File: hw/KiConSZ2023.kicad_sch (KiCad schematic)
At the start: 0 parts

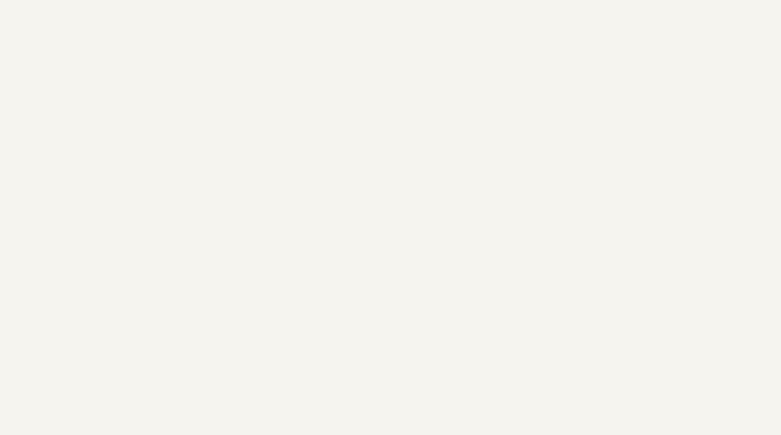
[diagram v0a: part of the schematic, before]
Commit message: USB Type-C Connector
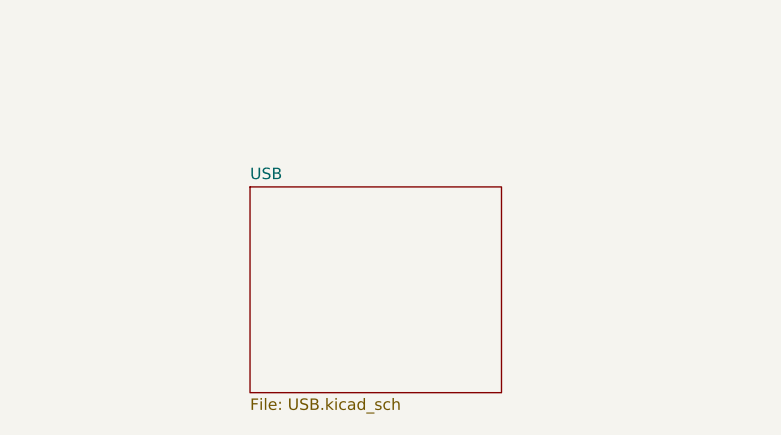
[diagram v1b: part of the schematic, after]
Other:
- added sheet USB (USB.kicad_sch)
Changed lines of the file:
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@@
     (effects (font (size 1.27 1.27)) (justify left bottom))
+  )
+  (sheet (at 45.72 167.64) (size 27.94 22.86) (fields_autoplaced)
+    (stroke (width 0.1524) (type solid))
+    (fill (color 0 0 0 0.0000))
+    (property "Sheetname" "USB" (at 45.72 166.9284 0)
+      (effects (font (size 1.27 1.27)) (justify left bottom))
+    )
+    (property "Sheetfile" "USB.kicad_sch" (at 45.72 191.0846 0)
+      (effects (font (size 1.27 1.27)) (justify left top))
+    )
+    (instances
+      (project "KiConSZ2023"
+        (path "/8659c260-f029-4e72-8b9a-85fff45eea40" (page "58"))
+      )
+    )
   )
   (sheet (at 177.8 48.26) (size 63.5 68.58) (fields_autoplaced)

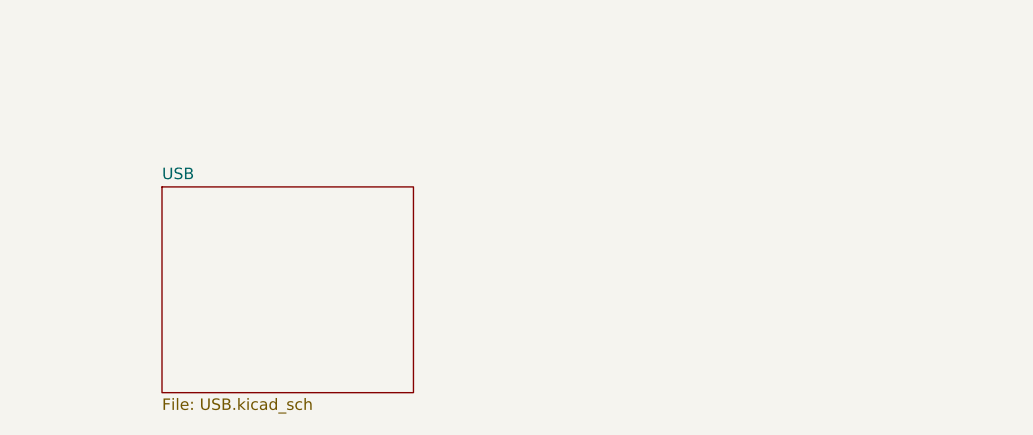
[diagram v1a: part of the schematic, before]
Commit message: added Buck Converter
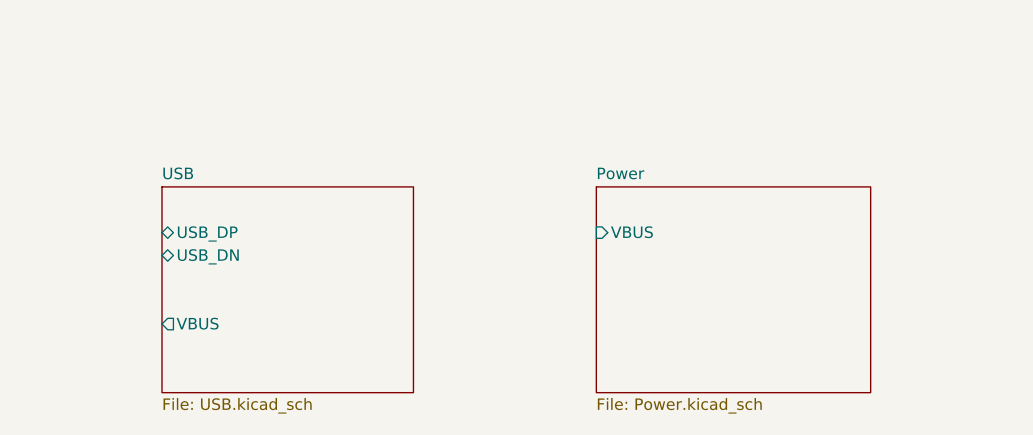
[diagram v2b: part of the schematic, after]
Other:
- added sheet Power (Power.kicad_sch)
- sheet USB ports: added USB_DN, USB_DP, VBUS; removed none
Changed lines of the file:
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@@
       (effects (font (size 1.27 1.27)) (justify left top))
+    )
+    (pin "USB_DP" bidirectional (at 45.72 172.72 180)
+      (effects (font (size 1.27 1.27)) (justify left))
+    )
+    (pin "VBUS" output (at 45.72 182.88 180)
+      (effects (font (size 1.27 1.27)) (justify left))
+    )
+    (pin "USB_DN" bidirectional (at 45.72 175.26 180)
+      (effects (font (size 1.27 1.27)) (justify left))
     )
     (instances
@@
       )
     )
+  )
+  (sheet (at 93.98 167.64) (size 30.48 22.86) (fields_autoplaced)
+    (stroke (width 0.1524) (type solid))
+    (fill (color 0 0 0 0.0000))
+    (property "Sheetname" "Power" (at 93.98 166.9284 0)
+      (effects (font (size 1.27 1.27)) (justify left bottom))
+    )
+    (property "Sheetfile" "Power.kicad_sch" (at 93.98 191.0846 0)
+      (effects (font (size 1.27 1.27)) (justify left top))
+    )
+    (pin "VBUS" input (at 93.98 172.72 180)
+      (effects (font (size 1.27 1.27)) (justify left))
+    )
+    (instances
+      (project "KiConSZ2023"
+        (path "/8659c260-f029-4e72-8b9a-85fff45eea40" (page "59"))
+      )
+    )

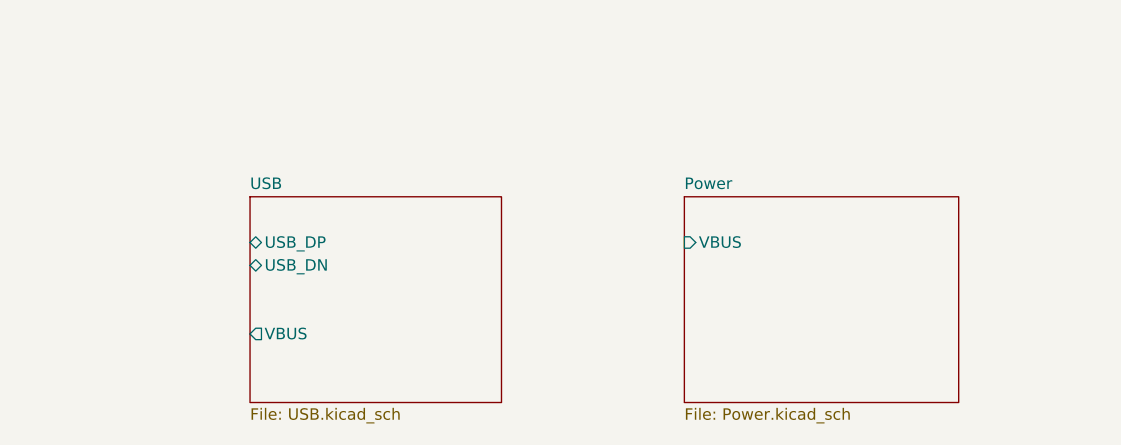
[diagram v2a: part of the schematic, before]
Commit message: added switches
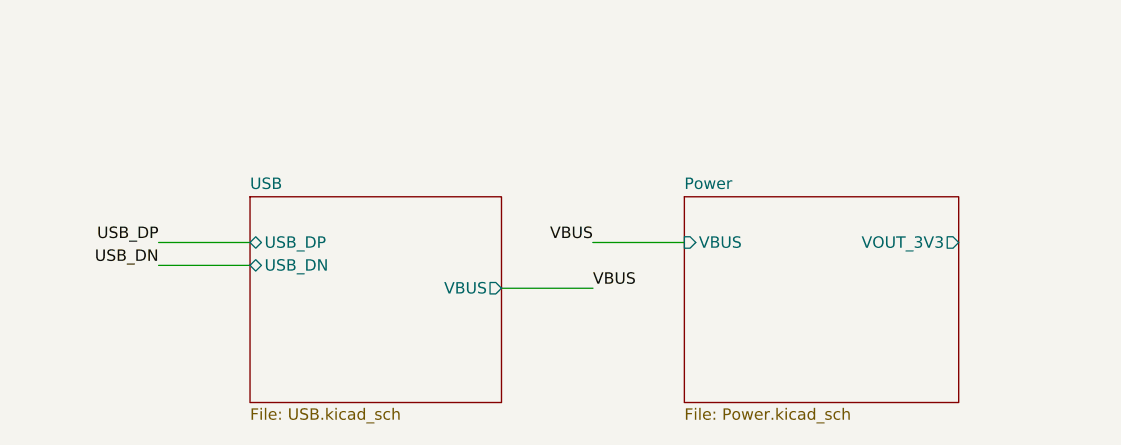
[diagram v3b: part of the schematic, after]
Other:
- sheet Power ports: added VOUT_3V3; removed none
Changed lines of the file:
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@@
+    (stroke (width 0) (type default))
+  )
+  (wire (pts (xy 45.72 175.26) (xy 35.56 175.26))
     (stroke (width 0) (type default))
   )
@@
     (stroke (width 0) (type default))
   )
+  (wire (pts (xy 83.82 172.72) (xy 93.98 172.72))
+    (stroke (width 0) (type default))
+  )
   (wire (pts (xy 241.3 106.68) (xy 248.92 106.68))
     (stroke (width 0) (type default))
@@
     (stroke (width 0) (type default))
   )
+  (wire (pts (xy 45.72 172.72) (xy 35.56 172.72))
+    (stroke (width 0) (type default))
+  )
   (wire (pts (xy 97.79 99.06) (xy 106.68 99.06))
     (stroke (width 0) (type default))
@@
     (stroke (width 0) (type default))
   )
+  (wire (pts (xy 83.82 177.8) (xy 73.66 177.8))
+    (stroke (width 0) (type default))
+  )
   (wire (pts (xy 43.18 96.52) (xy 33.02 96.52))
     (stroke (width 0) (type default))
@@
     (effects (font (size 1.27 1.27)) (justify left bottom))
   )
+  (label "USB_DN" (at 35.56 175.26 180) (fields_autoplaced)
+    (effects (font (size 1.27 1.27)) (justify right bottom))
+  )
+  (label "VBUS" (at 83.82 172.72 180) (fields_autoplaced)
+    (effects (font (size 1.27 1.27)) (justify right bottom))
+  )
   (label "DISP_SCK" (at 33.02 76.2 180) (fields_autoplaced)
     (effects (font (size 1.27 1.27)) (justify right bottom))
   )
+  (label "VBUS" (at 83.82 177.8 0) (fields_autoplaced)
+    (effects (font (size 1.27 1.27)) (justify left bottom))
+  )
   (label "LowSide_Input_B_Col_6" (at 106.68 132.08 0) (fields_autoplaced)
     (effects (font (size 1.27 1.27)) (justify left bottom))
@@
   (label "LowSide_Input_R_Col_2" (at 106.68 86.36 0) (fields_autoplaced)
     (effects (font (size 1.27 1.27)) (justify left bottom))
+  )
+  (label "USB_DP" (at 35.56 172.72 180) (fields_autoplaced)
+    (effects (font (size 1.27 1.27)) (justify right bottom))
   )
   (label "LowSide_Input_G_Col_1" (at 105.41 78.74 0) (fields_autoplaced)
@@
       (effects (font (size 1.27 1.27)) (justify left))
     )
-    (pin "VBUS" output (at 45.72 182.88 180)
-      (effects (font (size 1.27 1.27)) (justify left))
+    (pin "VBUS" output (at 73.66 177.8 0)
+      (effects (font (size 1.27 1.27)) (justify right))
     )
     (pin "USB_DN" bidirectional (at 45.72 175.26 180)
@@
       (effects (font (size 1.27 1.27)) (justify left))
     )
+    (pin "VOUT_3V3" output (at 124.46 172.72 0)
+      (effects (font (size 1.27 1.27)) (justify right))
+    )
     (instances

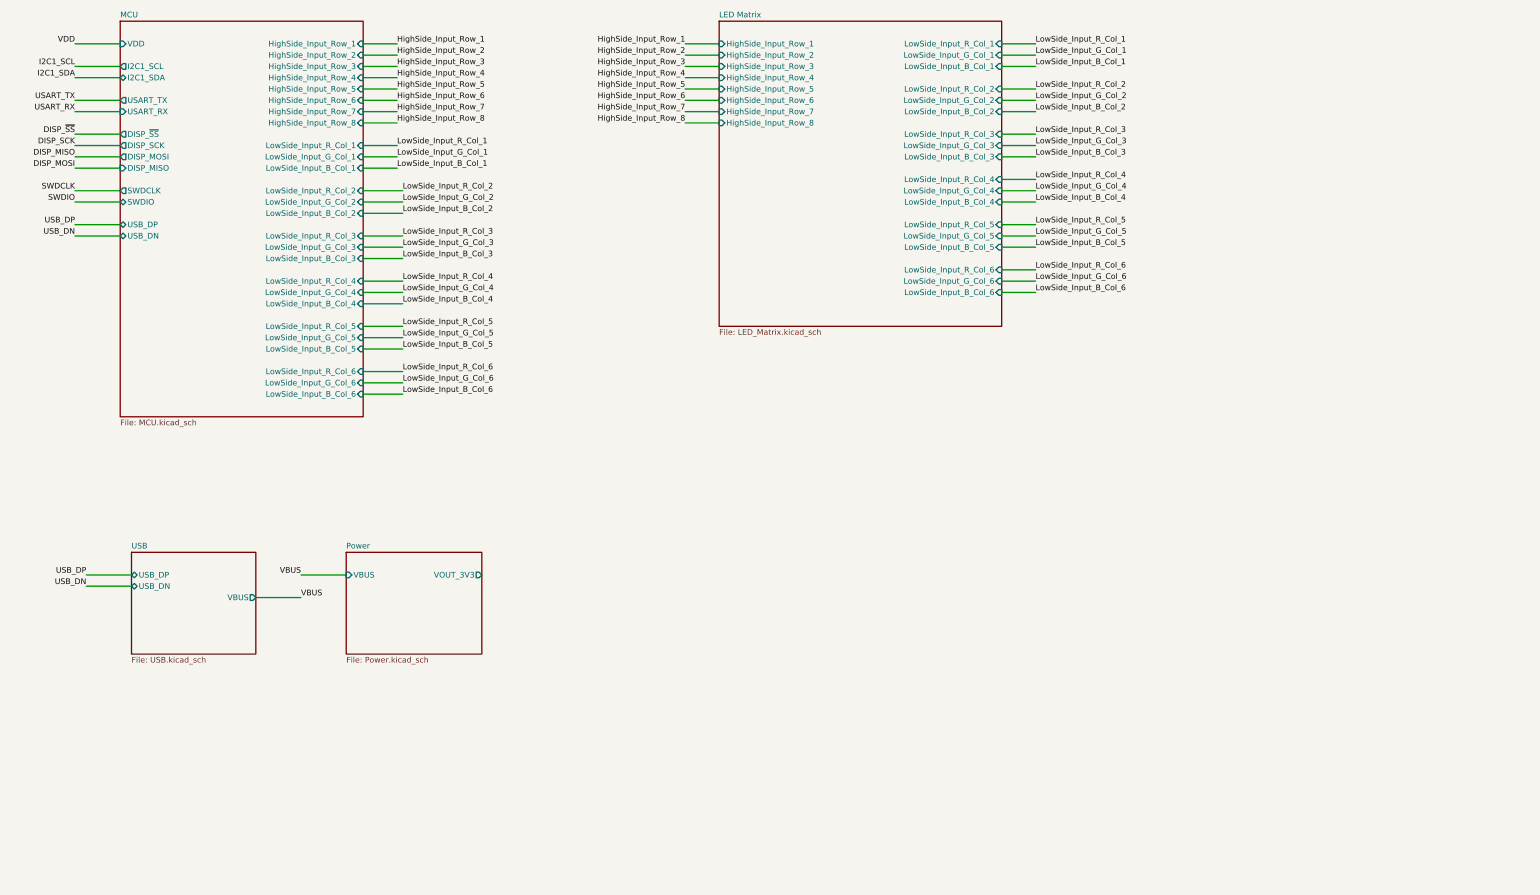
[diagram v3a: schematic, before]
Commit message: changed connections and ports
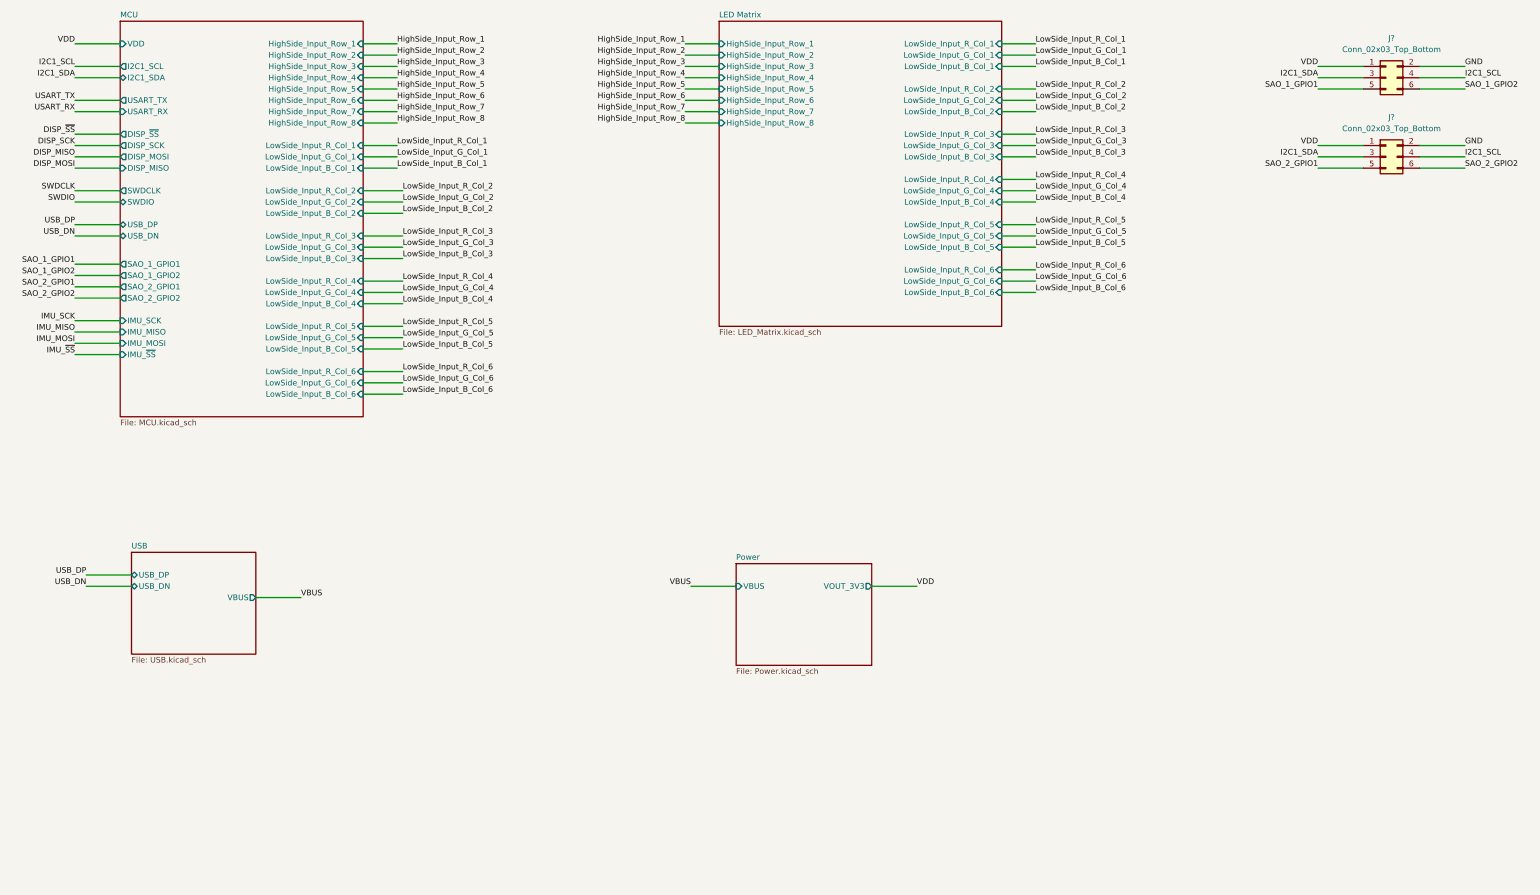
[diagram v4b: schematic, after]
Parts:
- added J? (x2): Conn_02x03_Top_Bottom, symbol Connector_Generic:Conn_02x03_Odd_Even
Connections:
- net I2C1_SCL: now also J?.4 (Pin_4), J?.4 (Pin_4)
- net I2C1_SDA: now also J?.3 (Pin_3), J?.3 (Pin_3)
- net VDD: now also J?.1 (Pin_1), J?.1 (Pin_1)
- new net GND: J?.2 (Pin_2), J?.2 (Pin_2)
- new net SAO_1_GPIO1: J?.5 (Pin_5)
- new net SAO_1_GPIO2: J?.6 (Pin_6)
- new net SAO_2_GPIO1: J?.5 (Pin_5)
- new net SAO_2_GPIO2: J?.6 (Pin_6)
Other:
- sheet MCU ports: added IMU_MISO, IMU_MOSI, IMU_SCK, IMU_~{SS}, SAO_1_GPIO1, SAO_1_GPIO2, SAO_2_GPIO1, SAO_2_GPIO2; removed none

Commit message: setup footprints of 02x03 SAO connectors
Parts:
- J? (x2): footprint (none) -> Connector_PinSocket_2.54mm:PinSocket_2x03_P2.54mm_Vertical
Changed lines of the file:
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@@
       (effects (font (size 1.27 1.27)))
     )
-    (property "Footprint" "" (at 327.66 78.74 0)
+    (property "Footprint" "Connector_PinSocket_2.54mm:PinSocket_2x03_P2.54mm_Vertical" (at 327.66 78.74 0)
       (effects (font (size 1.27 1.27)) hide)
     )
@@
       (effects (font (size 1.27 1.27)))
     )
-    (property "Footprint" "" (at 327.66 60.96 0)
+    (property "Footprint" "Connector_PinSocket_2.54mm:PinSocket_2x03_P2.54mm_Vertical" (at 327.66 60.96 0)
       (effects (font (size 1.27 1.27)) hide)
     )

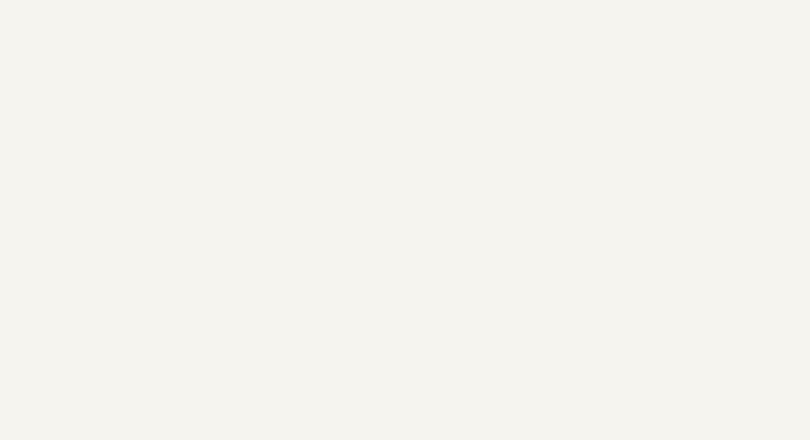
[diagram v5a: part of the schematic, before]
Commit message: added QMI8658A
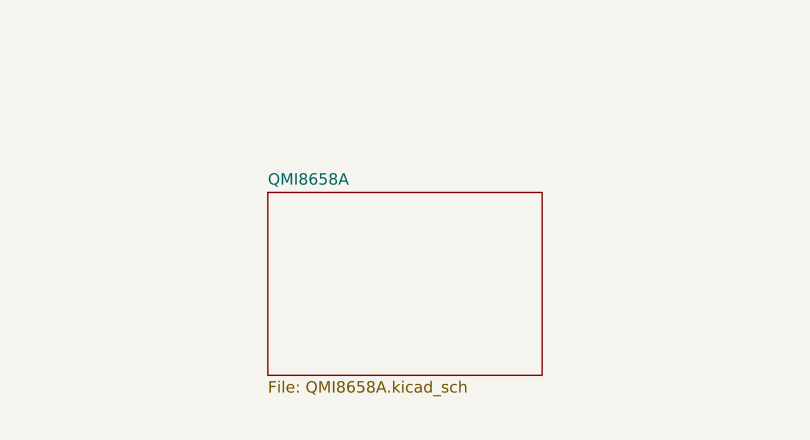
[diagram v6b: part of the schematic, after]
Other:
- added sheet QMI8658A (QMI8658A.kicad_sch)
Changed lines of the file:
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@@
+    )
+  )
+  (sheet (at 265.43 170.18) (size 30.48 20.32) (fields_autoplaced)
+    (stroke (width 0.1524) (type solid))
+    (fill (color 0 0 0 0.0000))
+    (property "Sheetname" "QMI8658A" (at 265.43 169.4684 0)
+      (effects (font (size 1.27 1.27)) (justify left bottom))
+    )
+    (property "Sheetfile" "QMI8658A.kicad_sch" (at 265.43 191.0846 0)
+      (effects (font (size 1.27 1.27)) (justify left top))
+    )
+    (instances
+      (project "KiConSZ2023"
+        (path "/8659c260-f029-4e72-8b9a-85fff45eea40" (page "62"))
+      )
     )
   )
